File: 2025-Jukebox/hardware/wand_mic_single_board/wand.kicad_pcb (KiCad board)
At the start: 4 copper layers, 17.5 x 63 mm, 53 parts, among them J1 USB_C_Receptacle_USB2.0, J4 Conn_01x02, J9 Conn_01x02, Q1 MUN5214DW1T1G, Q3 CJ3139K, SW1 SW_Push, U1 CP2104, U2 ESP32-PICO-D4, U4 TP4065-4.2V, U6 LY68L6400SLIT, U8 BNO055, U9 TLV76733DRVx, Y1 32.768kHz

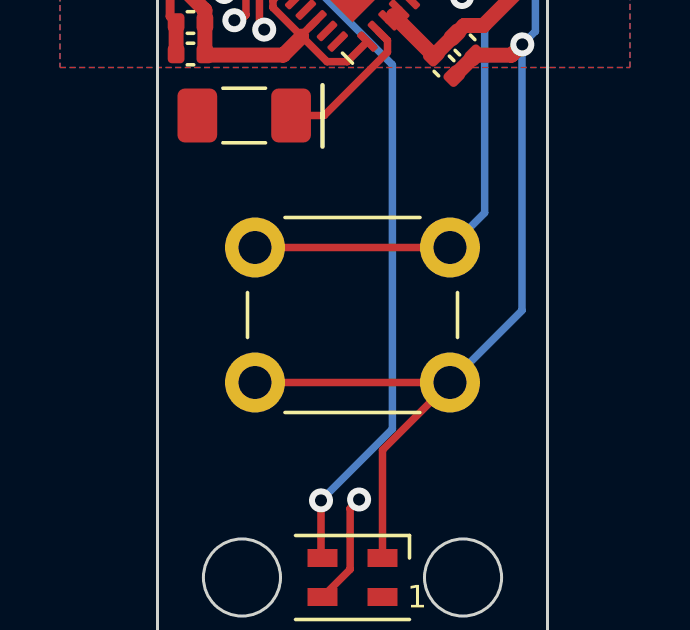
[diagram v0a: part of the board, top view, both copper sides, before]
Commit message: Changed button location
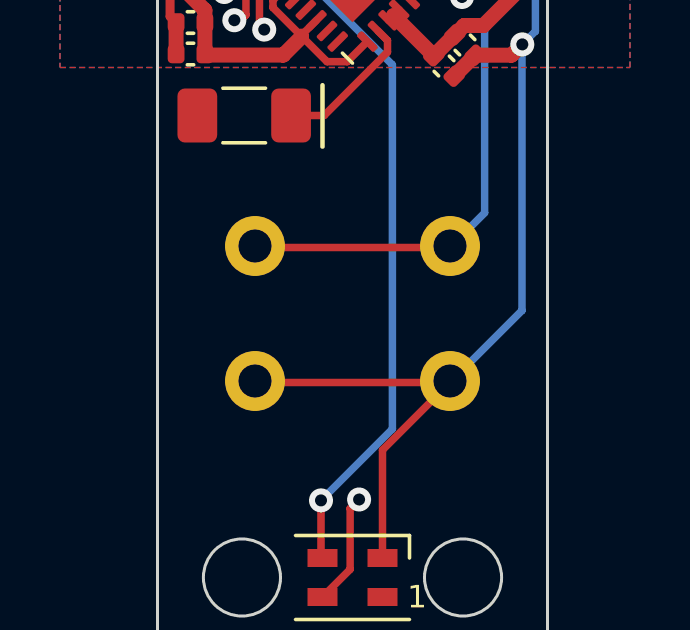
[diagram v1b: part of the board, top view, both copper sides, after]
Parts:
- SW1: footprint Button_Switch_THT:SW_PUSH_6mm -> Button_Switch_THT:SW_PUSH_6mm_H13mm; moved to B.Cu
- moved SW1 6.50 mm to (145.9, 116.1), turned to 180 degrees
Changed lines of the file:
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@@
-    )
-  )
-  (footprint "Button_Switch_THT:SW_PUSH_6mm" (layer "F.Cu")
-    (at 139.39 116.18375)
-    (descr "https://www.omron.com/ecb/products/pdf/en-b3f.pdf")
-    (tags "tact sw push 6mm")
-    (property "Sheetfile" "wand.kicad_sch")
-    (property "Sheetname" "")
-    (property "ki_description" "Push button switch, generic, two pins")
-    (property "ki_keywords" "switch normally-open pushbutton push-button")
-    (attr through_hole)
-    (fp_text reference "SW1" (at 3.25 -2) (layer "F.SilkS") hide
-        (effects (font (size 1 1) (thickness 0.15)))
-    )
-    (fp_text value "SW_Push" (at 3.75 6.7) (layer "F.Fab")
-        (effects (font (size 1 1) (thickness 0.15)))
-    )
-    (fp_text user "${REFERENCE}" (at 3.25 2.25) (layer "F.Fab")
-        (effects (font (size 1 1) (thickness 0.15)))
-    )
-    (fp_line (start -0.25 1.5) (end -0.25 3)
-      (stroke (width 0.12) (type solid)) (layer "F.SilkS"))
-    (fp_line (start 1 5.5) (end 5.5 5.5)
-      (stroke (width 0.12) (type solid)) (layer "F.SilkS"))
-    (fp_line (start 5.5 -1) (end 1 -1)
-      (stroke (width 0.12) (type solid)) (layer "F.SilkS"))
-    (fp_line (start 6.75 3) (end 6.75 1.5)
-      (stroke (width 0.12) (type solid)) (layer "F.SilkS"))
-    (fp_line (start -1.5 -1.5) (end -1.25 -1.5)
-      (stroke (width 0.05) (type solid)) (layer "F.CrtYd"))
-    (fp_line (start -1.5 -1.25) (end -1.5 -1.5)
-      (stroke (width 0.05) (type solid)) (layer "F.CrtYd"))
-    (fp_line (start -1.5 5.75) (end -1.5 -1.25)
-      (stroke (width 0.05) (type solid)) (layer "F.CrtYd"))
-    (fp_line (start -1.5 5.75) (end -1.5 6)
-      (stroke (width 0.05) (type solid)) (layer "F.CrtYd"))
-    (fp_line (start -1.5 6) (end -1.25 6)
-      (stroke (width 0.05) (type solid)) (layer "F.CrtYd"))
-    (fp_line (start -1.25 -1.5) (end 7.75 -1.5)
-      (stroke (width 0.05) (type solid)) (layer "F.CrtYd"))
-    (fp_line (start 7.75 -1.5) (end 8 -1.5)
-      (stroke (width 0.05) (type solid)) (layer "F.CrtYd"))
-    (fp_line (start 7.75 6) (end -1.25 6)
-      (stroke (width 0.05) (type solid)) (layer "F.CrtYd"))
-    (fp_line (start 7.75 6) (end 8 6)
-      (stroke (width 0.05) (type solid)) (layer "F.CrtYd"))
-    (fp_line (start 8 -1.5) (end 8 -1.25)
-      (stroke (width 0.05) (type solid)) (layer "F.CrtYd"))
-    (fp_line (start 8 -1.25) (end 8 5.75)
-      (stroke (width 0.05) (type solid)) (layer "F.CrtYd"))
-    (fp_line (start 8 6) (end 8 5.75)
-      (stroke (width 0.05) (type solid)) (layer "F.CrtYd"))
-    (fp_line (start 0.25 -0.75) (end 3.25 -0.75)
-      (stroke (width 0.1) (type solid)) (layer "F.Fab"))
-    (fp_line (start 0.25 5.25) (end 0.25 -0.75)
-      (stroke (width 0.1) (type solid)) (layer "F.Fab"))
-    (fp_line (start 3.25 -0.75) (end 6.25 -0.75)
-      (stroke (width 0.1) (type solid)) (layer "F.Fab"))
-    (fp_line (start 6.25 -0.75) (end 6.25 5.25)
-      (stroke (width 0.1) (type solid)) (layer "F.Fab"))
-    (fp_line (start 6.25 5.25) (end 0.25 5.25)
-      (stroke (width 0.1) (type solid)) (layer "F.Fab"))
-    (fp_circle (center 3.25 2.25) (end 1.25 2.5)
-      (stroke (width 0.1) (type solid)) (fill none) (layer "F.Fab"))
-    (pad "1" thru_hole circle (at 0 0 90) (size 2 2) (drill 1.1) (layers "*.Cu" "*.Mask")
-      (net 87 "Net-(U2-IO32)") (pinfunction "1") (pintype "passive"))
-    (pad "1" thru_hole circle (at 6.5 0 90) (size 2 2) (drill 1.1) (layers "*.Cu" "*.Mask")
-      (net 87 "Net-(U2-IO32)") (pinfunction "1") (pintype "passive"))
-    (pad "2" thru_hole circle (at 0 4.5 90) (size 2 2) (drill 1.1) (layers "*.Cu" "*.Mask")
-      (net 5 "GND") (pinfunction "2") (pintype "passive"))
-    (pad "2" thru_hole circle (at 6.5 4.5 90) (size 2 2) (drill 1.1) (layers "*.Cu" "*.Mask")
-      (net 5 "GND") (pinfunction "2") (pintype "passive"))
-    (model "${KICAD6_3DMODEL_DIR}/Button_Switch_THT.3dshapes/SW_PUSH_6mm.wrl"
-      (offset (xyz 0 0 0))
-      (scale (xyz 1 1 1))
-      (rotate (xyz 0 0 0))
     )
   )
@@
       (offset (xyz 0 0 0))
       (scale (xyz 1 1 1))
+      (rotate (xyz 0 0 0))
+    )
+  )
+  (footprint "Button_Switch_THT:SW_PUSH_6mm_H13mm" (layer "B.Cu")
+    (at 145.89 116.13375 180)
+    (descr "tactile push button, 6x6mm e.g. PHAP33xx series, height=13mm")
+    (tags "tact sw push 6mm")
+    (property "Sheetfile" "wand.kicad_sch")
+    (property "Sheetname" "")
+    (property "ki_description" "Push button switch, generic, two pins")
+    (property "ki_keywords" "switch normally-open pushbutton push-button")
+    (attr through_hole)
+    (fp_text reference "SW1" (at 3.25 2) (layer "B.SilkS") hide
+        (effects (font (size 1 1) (thickness 0.15)) (justify mirror))
+    )
+    (fp_text value "SW_Push" (at 3.75 -6.7) (layer "B.Fab")
+        (effects (font (size 1 1) (thickness 0.15)) (justify mirror))
+    )
+    (fp_text user "${REFERENCE}" (at 3.25 -2.25) (layer "B.Fab")
+        (effects (font (size 1 1) (thickness 0.15)) (justify mirror))
+    )
+    (fp_line (start -0.25 -1.5) (end -0.25 -3)
+      (stroke (width 0.12) (type solid)) (layer "B.SilkS"))
+    (fp_line (start 1 -5.5) (end 5.5 -5.5)
+      (stroke (width 0.12) (type solid)) (layer "B.SilkS"))
+    (fp_line (start 5.5 1) (end 1 1)
+      (stroke (width 0.12) (type solid)) (layer "B.SilkS"))
+    (fp_line (start 6.75 -3) (end 6.75 -1.5)
+      (stroke (width 0.12) (type solid)) (layer "B.SilkS"))
+    (fp_line (start -1.5 -6) (end -1.25 -6)
+      (stroke (width 0.05) (type solid)) (layer "B.CrtYd"))
+    (fp_line (start -1.5 -5.75) (end -1.5 -6)
+      (stroke (width 0.05) (type solid)) (layer "B.CrtYd"))
+    (fp_line (start -1.5 -5.75) (end -1.5 1.25)
+      (stroke (width 0.05) (type solid)) (layer "B.CrtYd"))
+    (fp_line (start -1.5 1.25) (end -1.5 1.5)
+      (stroke (width 0.05) (type solid)) (layer "B.CrtYd"))
+    (fp_line (start -1.5 1.5) (end -1.25 1.5)
+      (stroke (width 0.05) (type solid)) (layer "B.CrtYd"))
+    (fp_line (start -1.25 1.5) (end 7.75 1.5)
+      (stroke (width 0.05) (type solid)) (layer "B.CrtYd"))
+    (fp_line (start 7.75 -6) (end -1.25 -6)
+      (stroke (width 0.05) (type solid)) (layer "B.CrtYd"))
+    (fp_line (start 7.75 -6) (end 8 -6)
+      (stroke (width 0.05) (type solid)) (layer "B.CrtYd"))
+    (fp_line (start 7.75 1.5) (end 8 1.5)
+      (stroke (width 0.05) (type solid)) (layer "B.CrtYd"))
+    (fp_line (start 8 -6) (end 8 -5.75)
+      (stroke (width 0.05) (type solid)) (layer "B.CrtYd"))
+    (fp_line (start 8 1.25) (end 8 -5.75)
+      (stroke (width 0.05) (type solid)) (layer "B.CrtYd"))
+    (fp_line (start 8 1.5) (end 8 1.25)
+      (stroke (width 0.05) (type solid)) (layer "B.CrtYd"))
+    (fp_line (start 0.25 -5.25) (end 0.25 0.75)
+      (stroke (width 0.1) (type solid)) (layer "B.Fab"))
+    (fp_line (start 0.25 0.75) (end 3.25 0.75)
+      (stroke (width 0.1) (type solid)) (layer "B.Fab"))
+    (fp_line (start 3.25 0.75) (end 6.25 0.75)
+      (stroke (width 0.1) (type solid)) (layer "B.Fab"))
+    (fp_line (start 6.25 -5.25) (end 0.25 -5.25)
+      (stroke (width 0.1) (type solid)) (layer "B.Fab"))
+    (fp_line (start 6.25 0.75) (end 6.25 -5.25)
+      (stroke (width 0.1) (type solid)) (layer "B.Fab"))
+    (fp_circle (center 3.25 -2.25) (end 1.25 -2.5)
+      (stroke (width 0.1) (type solid)) (fill none) (layer "B.Fab"))
+    (pad "1" thru_hole circle (at 0 0 90) (size 2 2) (drill 1.1) (layers "*.Cu" "*.Mask")
+      (net 87 "Net-(U2-IO32)") (pinfunction "1") (pintype "passive"))
+    (pad "1" thru_hole circle (at 6.5 0 90) (size 2 2) (drill 1.1) (layers "*.Cu" "*.Mask")
+      (net 87 "Net-(U2-IO32)") (pinfunction "1") (pintype "passive"))
+    (pad "2" thru_hole circle (at 0 -4.5 90) (size 2 2) (drill 1.1) (layers "*.Cu" "*.Mask")
+      (net 5 "GND") (pinfunction "2") (pintype "passive"))
+    (pad "2" thru_hole circle (at 6.5 -4.5 90) (size 2 2) (drill 1.1) (layers "*.Cu" "*.Mask")
+      (net 5 "GND") (pinfunction "2") (pintype "passive"))
+    (model "${KICAD6_3DMODEL_DIR}/Button_Switch_THT.3dshapes/SW_PUSH_6mm_H13mm.wrl"
+      (offset (xyz 0 0 0))
+      (scale (xyz 1 1 1))
